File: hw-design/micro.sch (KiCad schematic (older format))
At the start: 32 parts

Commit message: Routing
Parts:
- added P6, P7: CONN_01X05, w_pin_strip:pin_strip_5, symbol CONN_01X05
- D1, D2, D3, D4: renamed from D?; footprint LEDs:LED-0603 -> LEDs:LED_0603
- R5, R7: renamed from R?; footprint (none) -> w_smd_resistors:r_0603
- Y1: renamed from Y?; footprint Crystals_Oscillators_SMD:crystal_FA238-TSX3225 -> Crystals:crystal_FA238-TSX3225
- gave numbers to parts that had none: 25
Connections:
- net +3V3: now also P7.5 (P5)
- net GND: now also P6.5 (P5)
- net complete: no longer U1.2 (PC13)
- net progress: no longer U1.46 (PB9)
- net at U1.29 (PA8): now also P7.2 (P2)
- net head2: now reaches U1.3 (PC14-OSC32_IN)
- net head2: now also P7.4 (P4)
- net at U1.30 (PA9): now also P7.1 (P1)
- net at U1.43 (PB7): now also P6.4 (P4)
- net at U1.44 (BOOT0-PF11): now also P6.3 (P3)
- net at U1.45 (PB8): now also P6.2 (P2)
- new net: P6.1 (P1), U1.46 (PB9)
- new net head1: P7.3 (P3), U1.2 (PC13)
- no-connect marks 2 -> 4
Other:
- moved on the sheet: C5, C6, C7

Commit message: patlabor logo
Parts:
- added P10: CONN_01X01, iwasz:patlabor1, symbol CONN_01X01
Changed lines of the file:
@@
 Text Label 4950 3700 2    60   ~ 0
 head2
+$Comp
+L CONN_01X01 P10
+U 1 1 5729A89D
+P 1475 1550
+F 0 "P10" H 1553 1591 50  0000 L CNN
+F 1 "CONN_01X01" H 1553 1500 50  0000 L CNN
+F 2 "iwasz:patlabor1" H 1475 1550 50  0001 C CNN
+F 3 "" H 1475 1550 50  0000 C CNN
+	1    1475 1550
+	1    0    0    -1
+$EndComp
 $EndSCHEMATC

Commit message: Some changes in HW. Dunno.
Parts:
- R6: value R -> 220R
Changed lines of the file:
@@
 P 4675 4000
 F 0 "R6" V 4755 4000 50  0000 C CNN
-F 1 "R" V 4675 4000 50  0000 C CNN
+F 1 "220R" V 4675 4000 50  0000 C CNN
 F 2 "w_smd_resistors:r_0603" V 4605 4000 30  0001 C CNN
 F 3 "" H 4675 4000 30  0000 C CNN

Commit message: Motors spin
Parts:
- removed P10: CONN_01X01, iwasz:patlabor1, symbol CONN_01X01
- U1: value STM32F072CB / STM32F042C6 -> STM32F072CB/F042C6
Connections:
- net aenblr: now also U1.21 (PB10); no longer U1.20 (PB2)
- net benblr: now also U1.22 (PB11); no longer U1.21 (PB10)
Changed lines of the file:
@@
 P 6000 4050
 F 0 "U1" H 6000 3700 60  0000 C CNN
-F 1 "STM32F072CB / STM32F042C6" H 6000 3600 60  0000 C CNN
+F 1 "STM32F072CB/F042C6" H 6000 3600 60  0000 C CNN
 F 2 "w_smd_lqfp:lqfp48" H 6450 3750 60  0001 C CNN
 F 3 "" H 6450 3750 60  0000 C CNN
@@
 Text HLabel 6050 5250 3    60   Output ~ 0
 benbll
-Text HLabel 6150 5250 3    60   Output ~ 0
+Text HLabel 6250 5250 3    60   Output ~ 0
 aenblr
-Text HLabel 6250 5250 3    60   Output ~ 0
+Text HLabel 6350 5250 3    60   Output ~ 0
 benblr
 Wire Wire Line
 	6050 5050 6050 5250
-Wire Wire Line
-	6150 5050 6150 5250
 Wire Wire Line
 	6250 5050 6250 5250
@@
 Text Label 7000 4300 0    60   ~ 0
 led4
-NoConn ~ 6350 5050
+NoConn ~ 6150 5050
 NoConn ~ 4950 3800
 Wire Wire Line
@@
 Text Label 4950 3700 2    60   ~ 0
 head2
-$Comp
-L CONN_01X01 P10
-U 1 1 5729A89D
-P 1475 1550
-F 0 "P10" H 1553 1591 50  0000 L CNN
-F 1 "CONN_01X01" H 1553 1500 50  0000 L CNN
-F 2 "iwasz:patlabor1" H 1475 1550 50  0001 C CNN
-F 3 "" H 1475 1550 50  0000 C CNN
-	1    1475 1550
-	1    0    0    -1
-$EndComp
+Wire Wire Line
+	6350 5050 6350 5250
 $EndSCHEMATC

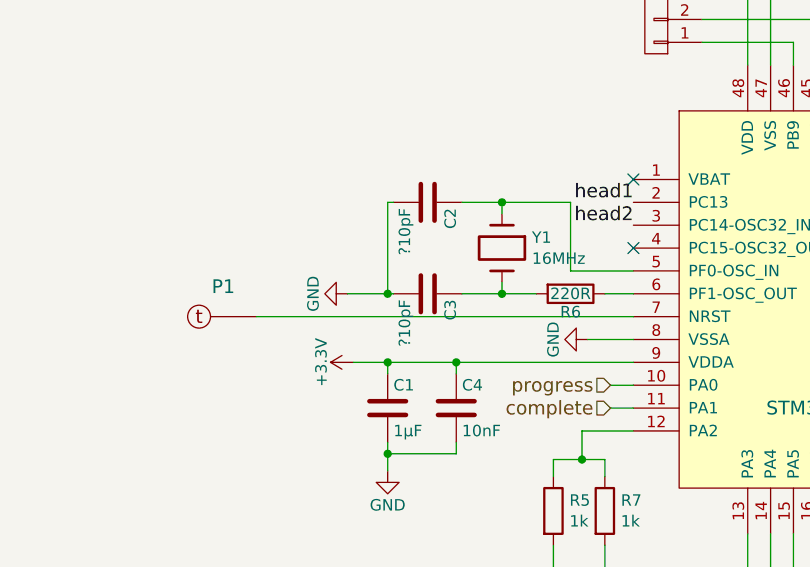
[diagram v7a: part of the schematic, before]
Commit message: BT turned of/on #define
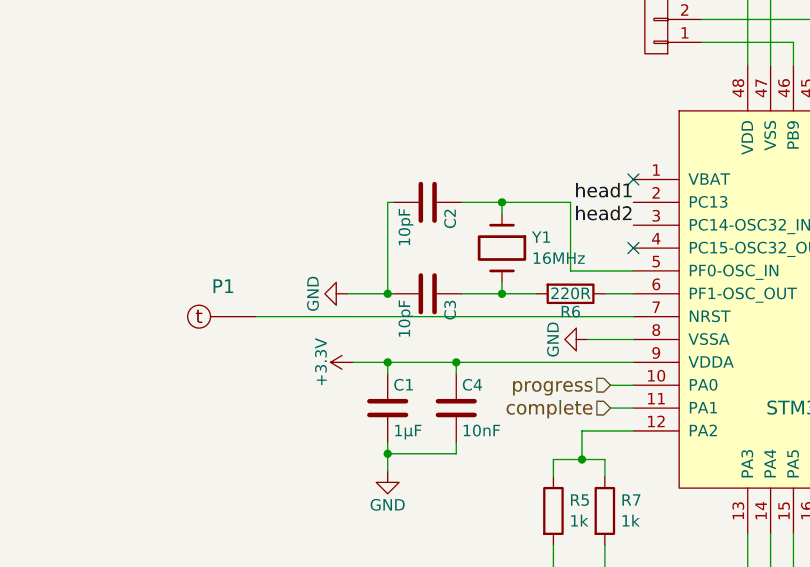
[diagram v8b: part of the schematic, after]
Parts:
- C2, C3: value ?10pF -> 10pF
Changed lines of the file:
@@
 F 1 "STM32F072CB/F042C6" H 6000 3600 60  0000 C CNN
 F 2 "w_smd_lqfp:lqfp48" H 6450 3750 60  0001 C CNN
-F 3 "" H 6450 3750 60  0000 C CNN
+F 3 "http://pl.rs-online.com/web/p/mikrokontrolery/7925921/" H 6450 3750 60  0001 C CNN
 F 4 "µC" H 6000 4050 60  0001 C CNN "Opis"
 	1    6000 4050
@@
 F 1 "16MHz" V 4421 3931 50  0000 L CNN
 F 2 "Crystals:crystal_FA238-TSX3225" H 4375 3800 60  0001 C CNN
-F 3 "" H 4375 3800 60  0000 C CNN
+F 3 "http://pl.farnell.com/abracon/abm8-16-000mhz-10-1-u-t/crystal-16mhz-10pf-3-2-x-2-5mm/dp/2467830" H 4375 3800 60  0001 C CNN
 	1    4375 3800
 	0    1    1    0
@@
 P 4050 4000
 F 0 "C3" H 4075 4100 50  0000 L CNN
-F 1 "?10pF" H 4075 3900 50  0000 L CNN
+F 1 "10pF" H 4075 3900 50  0000 L CNN
 F 2 "w_smd_cap:c_0603" H 4088 3850 30  0001 C CNN
 F 3 "" H 4050 4000 60  0000 C CNN
@@
 P 4050 3600
 F 0 "C2" H 4075 3700 50  0000 L CNN
-F 1 "?10pF" H 4075 3500 50  0000 L CNN
+F 1 "10pF" H 4075 3500 50  0000 L CNN
 F 2 "w_smd_cap:c_0603" H 4088 3450 30  0001 C CNN
 F 3 "" H 4050 3600 60  0000 C CNN
